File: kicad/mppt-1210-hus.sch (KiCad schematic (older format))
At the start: 6 parts

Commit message: Small changes and files renamed
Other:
- note added: "12V / 10A MPPT Solar Charge Controller with USB"
- note removed: "10A MPPT Solar Charge Controller with USB"
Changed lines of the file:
@@
 EESchema Schematic File Version 4
-LIBS:mppt-10a-cache
+LIBS:mppt-1210-hus-cache
 EELAYER 29 0
 EELAYER END
@@
 Sheet 1 4
 Title "10A MPPT Charge Controller with USB"
-Date "2019-04-09"
-Rev "0.6"
+Date "2019-06-03"
+Rev "0.6.1"
 Comp "Libre Solar / Connected Energy"
 Comment1 "Author: Martin Jäger"
@@
 F1 "power_supply.sch" 50
 $EndSheet
-Text Notes 2300 1500 0    200  ~ 0
-10A MPPT Solar Charge Controller with USB
+Text Notes 2000 1500 0    200  ~ 0
+12V / 10A MPPT Solar Charge Controller with USB
 Text Notes 2600 4700 0    100  ~ 0
 Main Specifications

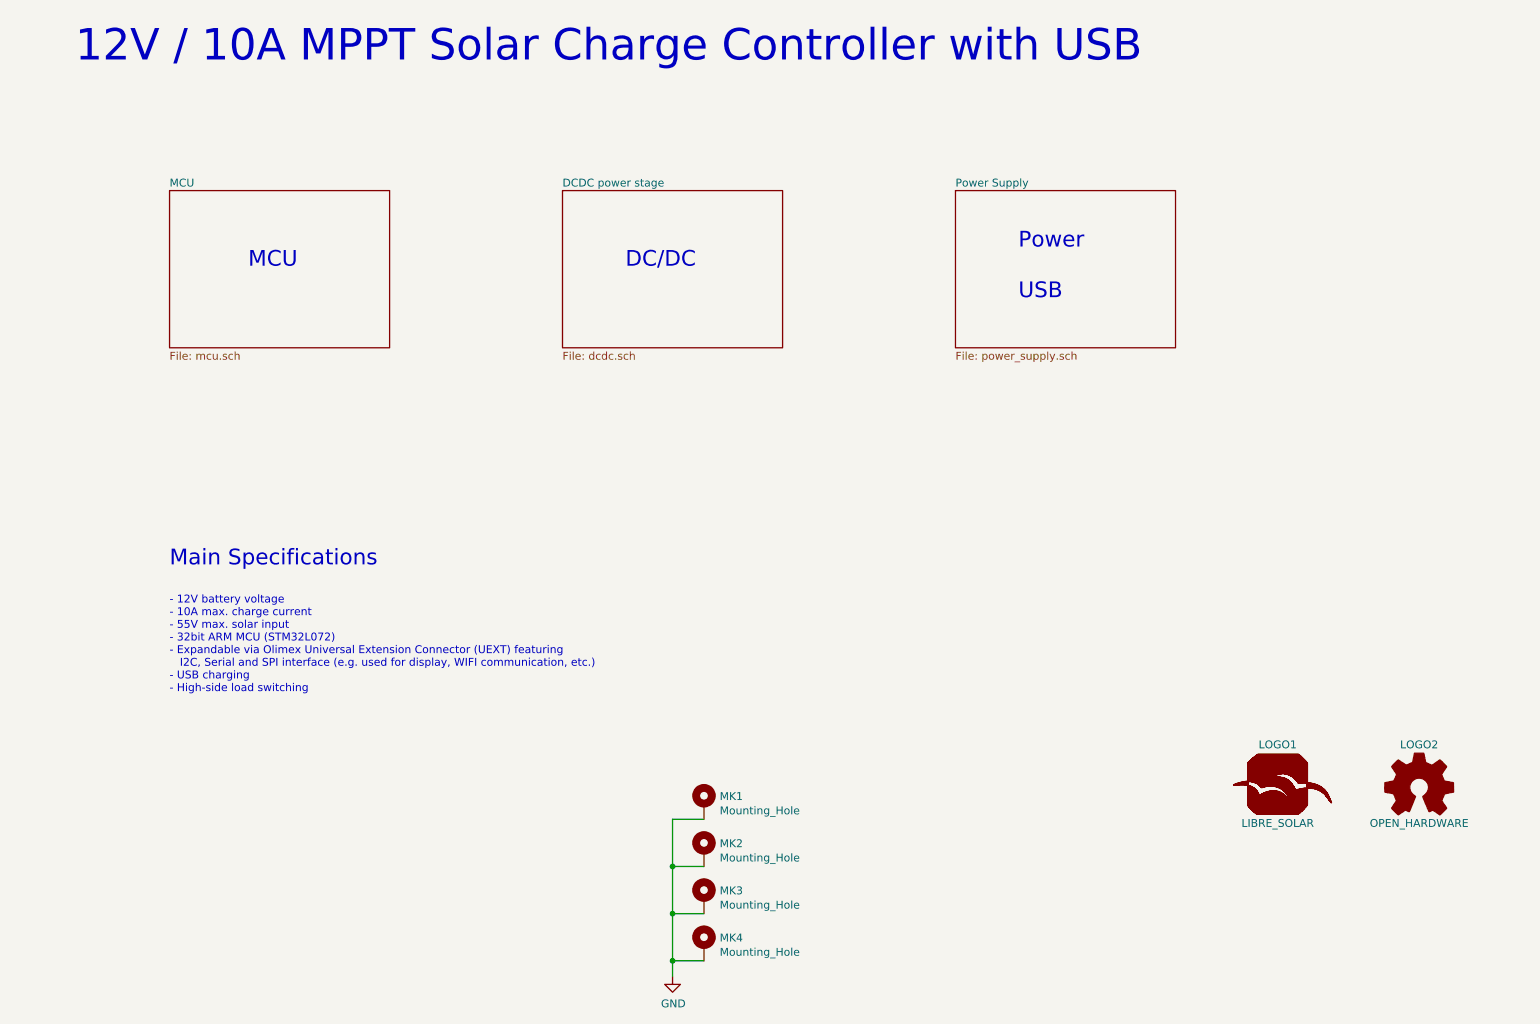
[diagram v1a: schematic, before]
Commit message: Small adjustments after testing
- MOSFET gate driver changed to reduce switch node ringing
- Current measurement output filter time constant reduced to have less delay
- BTN pin allows starting the bootloader if pulled to 3V3 before startup
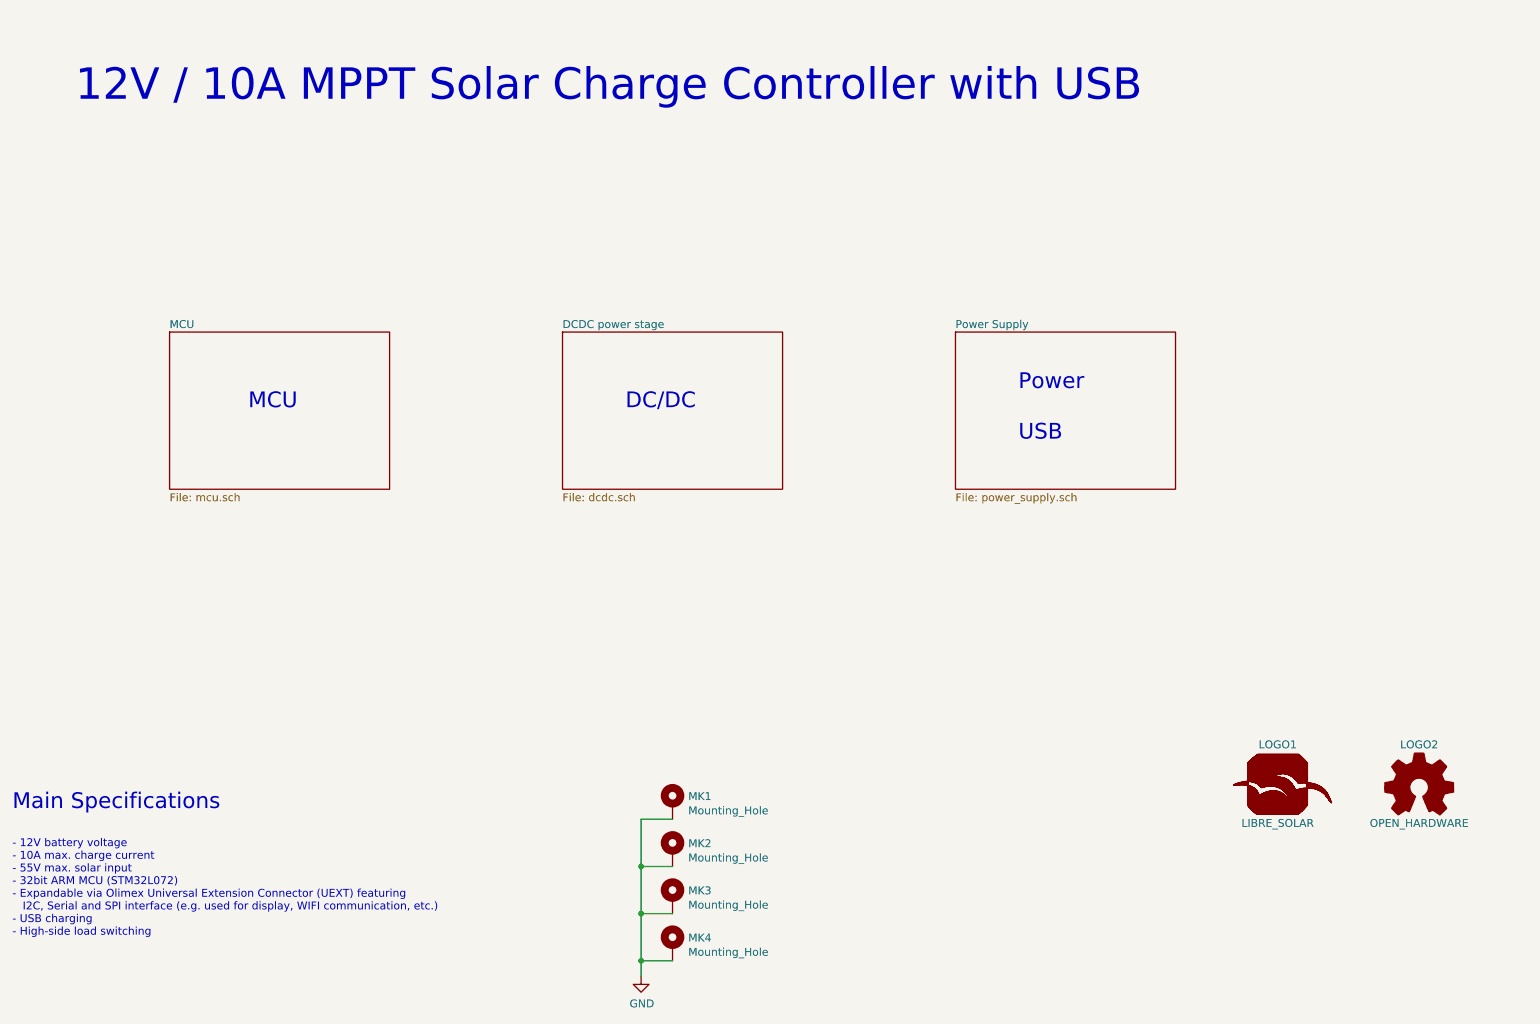
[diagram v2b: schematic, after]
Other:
- moved on the sheet: MK1, MK2, MK3, MK4
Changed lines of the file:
@@
 encoding utf-8
 Sheet 1 4
-Title "10A MPPT Charge Controller with USB"
-Date "2019-06-03"
-Rev "0.6.1"
-Comp "Libre Solar / Connected Energy"
+Title "MPPT 1210 HUS"
+Date "2019-07-24"
+Rev "0.7.1"
+Comp "Libre Solar"
 Comment1 "Author: Martin Jäger"
 Comment2 "Website: https://libre.solar"
@@
 $EndDescr
 $Sheet
-S 5100 2300 1400 1000
+S 5100 3200 1400 1000
 U 58A68DC9
 F0 "DCDC power stage" 50
@@
 $EndSheet
 $Sheet
-S 2600 2300 1400 1000
+S 2600 3200 1400 1000
 U 58A68DCB
 F0 "MCU" 50
@@
 $EndSheet
 $Sheet
-S 7600 2300 1400 1000
+S 7600 3200 1400 1000
 U 58C18D5C
 F0 "Power Supply" 50
 F1 "power_supply.sch" 50
 $EndSheet
-Text Notes 2000 1500 0    200  ~ 0
+Text Notes 2000 1750 0    200  ~ 0
 12V / 10A MPPT Solar Charge Controller with USB
-Text Notes 2600 4700 0    100  ~ 0
+Text Notes 1600 6250 0    100  ~ 0
 Main Specifications
-Text Notes 2600 5500 0    50   ~ 0
+Text Notes 1600 7050 0    50   ~ 0
 - 12V battery voltage\n- 10A max. charge current\n- 55V max. solar input\n- 32bit ARM MCU (STM32L072)\n- Expandable via Olimex Universal Extension Connector (UEXT) featuring\n   I2C, Serial and SPI interface (e.g. used for display, WIFI communication, etc.)\n- USB charging\n- High-side load switching\n
 $Comp
@@
 	1    0    0    -1
 $EndComp
-Text Notes 5500 2800 0    100  ~ 0
+Text Notes 5500 3700 0    100  ~ 0
 DC/DC
-Text Notes 3100 2800 0    100  ~ 0
+Text Notes 3100 3700 0    100  ~ 0
 MCU
-Text Notes 8000 3000 0    100  ~ 0
+Text Notes 8000 3900 0    100  ~ 0
 Power\n\nUSB
 $Comp
 L Mechanical:MountingHole_Pad MK1
 U 1 1 595388B0
-P 6000 6200
-F 0 "MK1" H 6100 6246 50  0000 L CNN
-F 1 "Mounting_Hole" H 6100 6155 50  0000 L CNN
-F 2 "MountingHole:MountingHole_3.2mm_M3_Pad" H 6000 6200 50  0001 C CNN
-F 3 "" H 6000 6200 50  0001 C CNN
-F 4 "+info" H 0   0   50  0001 C CNN "Config"
-	1    6000 6200
+P 5800 6200
+F 0 "MK1" H 5900 6246 50  0000 L CNN
+F 1 "Mounting_Hole" H 5900 6155 50  0000 L CNN
+F 2 "MountingHole:MountingHole_3.2mm_M3_Pad" H 5800 6200 50  0001 C CNN
+F 3 "" H 5800 6200 50  0001 C CNN
+F 4 "+info" H -200 0   50  0001 C CNN "Config"
+	1    5800 6200
 	1    0    0    -1
 $EndComp
@@
 L Mechanical:MountingHole_Pad MK2
 U 1 1 59538A86
-P 6000 6500
-F 0 "MK2" H 6100 6546 50  0000 L CNN
-F 1 "Mounting_Hole" H 6100 6455 50  0000 L CNN
-F 2 "MountingHole:MountingHole_3.2mm_M3_Pad" H 6000 6500 50  0001 C CNN
-F 3 "" H 6000 6500 50  0001 C CNN
-F 4 "+info" H 0   0   50  0001 C CNN "Config"
-	1    6000 6500
+P 5800 6500
+F 0 "MK2" H 5900 6546 50  0000 L CNN
+F 1 "Mounting_Hole" H 5900 6455 50  0000 L CNN
+F 2 "MountingHole:MountingHole_3.2mm_M3_Pad" H 5800 6500 50  0001 C CNN
+F 3 "" H 5800 6500 50  0001 C CNN
+F 4 "+info" H -200 0   50  0001 C CNN "Config"
+	1    5800 6500
 	1    0    0    -1
 $EndComp
@@
 L Mechanical:MountingHole_Pad MK3
 U 1 1 59538C18
-P 6000 6800
-F 0 "MK3" H 6100 6846 50  0000 L CNN
-F 1 "Mounting_Hole" H 6100 6755 50  0000 L CNN
-F 2 "MountingHole:MountingHole_3.2mm_M3_Pad" H 6000 6800 50  0001 C CNN
-F 3 "" H 6000 6800 50  0001 C CNN
-F 4 "+info" H 0   0   50  0001 C CNN "Config"
-	1    6000 6800
+P 5800 6800
+F 0 "MK3" H 5900 6846 50  0000 L CNN
+F 1 "Mounting_Hole" H 5900 6755 50  0000 L CNN
+F 2 "MountingHole:MountingHole_3.2mm_M3_Pad" H 5800 6800 50  0001 C CNN
+F 3 "" H 5800 6800 50  0001 C CNN
+F 4 "+info" H -200 0   50  0001 C CNN "Config"
+	1    5800 6800
 	1    0    0    -1
 $EndComp
 Wire Wire Line
-	6000 6300 5800 6300
+	5800 6300 5600 6300
 Wire Wire Line
-	5800 6300 5800 6600
+	5600 6300 5600 6600
 Wire Wire Line
-	5800 6600 6000 6600
+	5600 6600 5800 6600
 Wire Wire Line
-	5800 6600 5800 6900
+	5600 6600 5600 6900
 Wire Wire Line
-	5800 6900 6000 6900
-Connection ~ 5800 6600
+	5600 6900 5800 6900
+Connection ~ 5600 6600
 $Comp
 L power:GND #PWR0106
 U 1 1 5AF1E99A
-P 5800 7300
-F 0 "#PWR0106" H 5800 7050 50  0001 C CNN
-F 1 "GND" H 5805 7127 50  0000 C CNN
-F 2 "" H 5800 7300 50  0001 C CNN
-F 3 "" H 5800 7300 50  0001 C CNN
-	1    5800 7300
+P 5600 7300
+F 0 "#PWR0106" H 5600 7050 50  0001 C CNN
+F 1 "GND" H 5605 7127 50  0000 C CNN
+F 2 "" H 5600 7300 50  0001 C CNN
+F 3 "" H 5600 7300 50  0001 C CNN
+	1    5600 7300
 	1    0    0    -1
 $EndComp
-Connection ~ 5800 6900
+Connection ~ 5600 6900
 $Comp
 L Mechanical:MountingHole_Pad MK4
 U 1 1 5B038156
-P 6000 7100
-F 0 "MK4" H 6100 7146 50  0000 L CNN
-F 1 "Mounting_Hole" H 6100 7055 50  0000 L CNN
-F 2 "MountingHole:MountingHole_3.2mm_M3_Pad" H 6000 7100 50  0001 C CNN
-F 3 "" H 6000 7100 50  0001 C CNN
-F 4 "+info" H 0   0   50  0001 C CNN "Config"
-	1    6000 7100
+P 5800 7100
+F 0 "MK4" H 5900 7146 50  0000 L CNN
+F 1 "Mounting_Hole" H 5900 7055 50  0000 L CNN
+F 2 "MountingHole:MountingHole_3.2mm_M3_Pad" H 5800 7100 50  0001 C CNN
+F 3 "" H 5800 7100 50  0001 C CNN
+F 4 "+info" H -200 0   50  0001 C CNN "Config"
+	1    5800 7100
 	1    0    0    -1
 $EndComp
 Wire Wire Line
-	5800 6900 5800 7200
+	5600 6900 5600 7200
 Wire Wire Line
-	6000 7200 5800 7200
-Connection ~ 5800 7200
+	5800 7200 5600 7200
+Connection ~ 5600 7200
 Wire Wire Line
-	5800 7200 5800 7300
+	5600 7200 5600 7300
 $EndSCHEMATC
